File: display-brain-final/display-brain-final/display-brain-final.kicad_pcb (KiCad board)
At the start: 2 copper layers, 104.2 x 68 mm, 22 parts, among them J1 Conn_01x02_Socket, J2 Conn_01x05_Socket, J3 Conn_01x19_Socket, J4 Conn_01x19_Socket, J5 Conn_01x04_Socket, J6 Conn_01x05_Socket, J7 Conn_01x02_Socket, P1 USB_C_Plug_USB2.0, U3 AMS1117CD-3.3

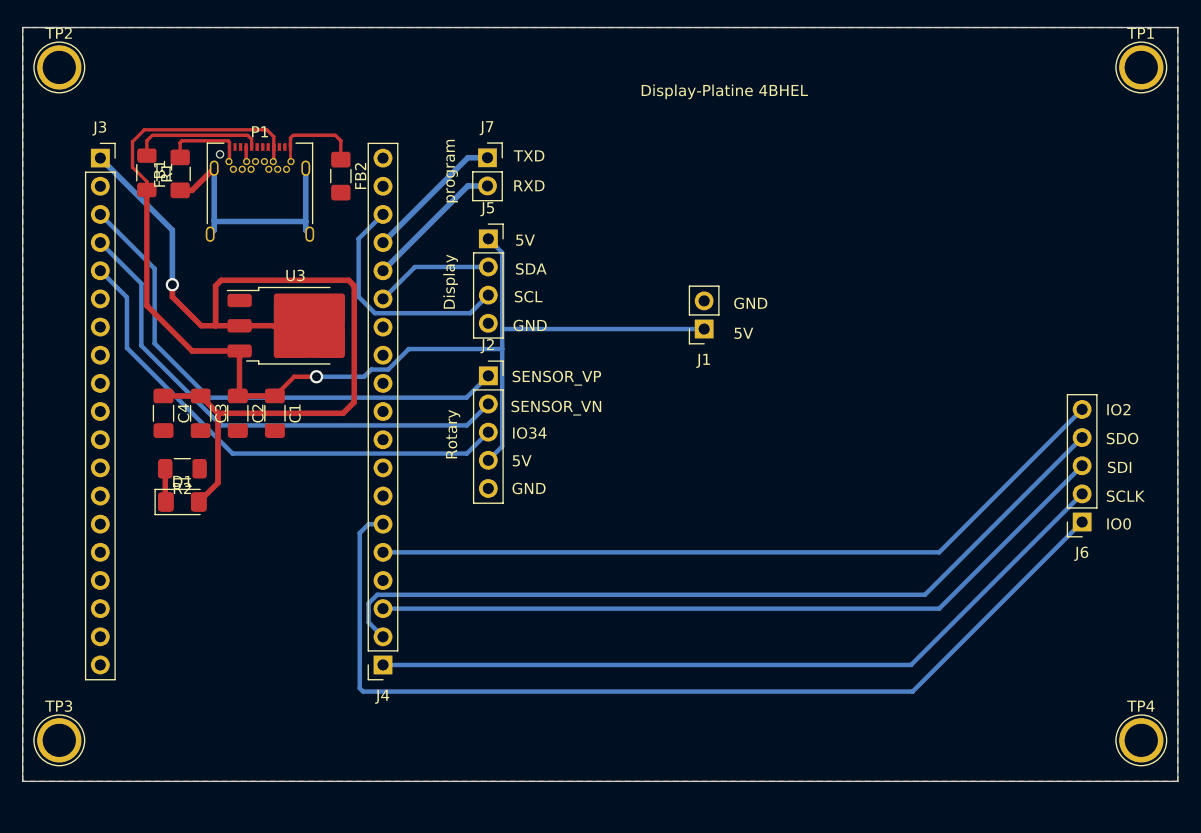
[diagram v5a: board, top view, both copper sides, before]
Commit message: Replaced ASM1117 with LM317 in schematic.
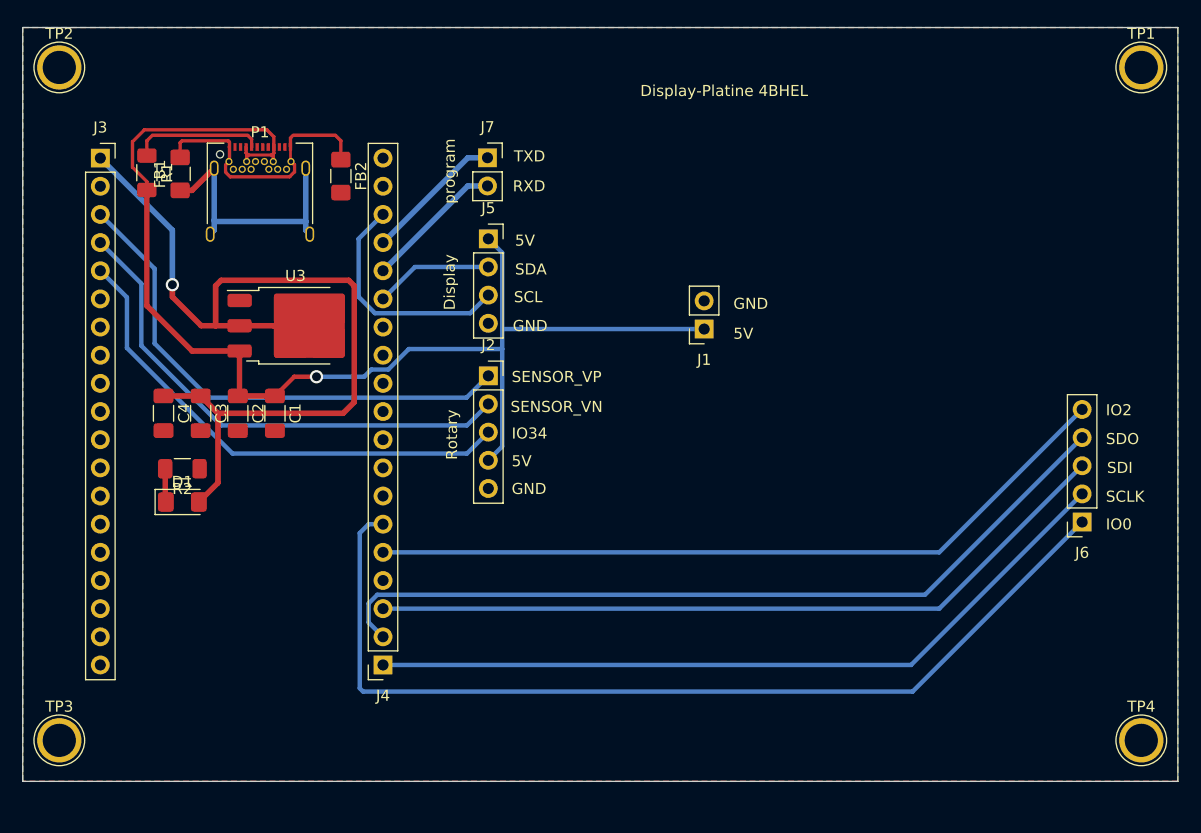
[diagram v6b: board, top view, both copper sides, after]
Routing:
- net Net-(FB1-Pad2): track 16.4 -> 25.0 mm
- net /5V: track 111.4 -> 113.5 mm
- net /SD1: track 69.0 -> 68.4 mm
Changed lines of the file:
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@@
   (segment (start 140.47 58.92) (end 140.3 59.09) (width 0.3) (layer "F.Cu") (net 2))
   (segment (start 140.3 59.09) (end 140.3 60.4125) (width 0.3) (layer "F.Cu") (net 2))
+  (segment (start 144.7 60.79) (end 144.399 61.091) (width 0.3) (layer "F.Cu") (net 2))
   (segment (start 150.25 58.665) (end 150.495 58.42) (width 0.3) (layer "F.Cu") (net 2))
+  (segment (start 150.622 61.087) (end 150.597 61.087) (width 0.3) (layer "F.Cu") (net 2))
+  (segment (start 144.399 61.091) (end 144.399 61.743595) (width 0.3) (layer "F.Cu") (net 2))
   (segment (start 150.495 58.42) (end 154.305 58.42) (width 0.3) (layer "F.Cu") (net 2))
+  (segment (start 150.179 62.165) (end 150.622 61.722) (width 0.3) (layer "F.Cu") (net 2))
   (segment (start 144.75 59.48) (end 144.75 60.74) (width 0.3) (layer "F.Cu") (net 2))
+  (segment (start 150.622 61.722) (end 150.622 61.087) (width 0.3) (layer "F.Cu") (net 2))
   (segment (start 154.305 58.42) (end 154.8 58.915) (width 0.3) (layer "F.Cu") (net 2))
-  (segment (start 144.75 60.74) (end 144.7 60.79) (width 0.3) (layer "F.Cu") (net 2))
+  (segment (start 144.399 61.743595) (end 144.820405 62.165) (width 0.3) (layer "F.Cu") (net 2))
   (segment (start 150.25 60.74) (end 150.25 59.48) (width 0.25) (layer "F.Cu") (net 2))
-  (segment (start 150.3 60.79) (end 150.25 60.74) (width 0.25) (layer "F.Cu") (net 2))
   (segment (start 154.8 58.915) (end 154.8 60.6125) (width 0.3) (layer "F.Cu") (net 2))
   (segment (start 144.75 59.025) (end 144.645 58.92) (width 0.3) (layer "F.Cu") (net 2))
+  (segment (start 150.597 61.087) (end 150.3 60.79) (width 0.3) (layer "F.Cu") (net 2))
   (segment (start 144.75 59.48) (end 144.75 59.025) (width 0.3) (layer "F.Cu") (net 2))
+  (segment (start 144.820405 62.165) (end 150.179 62.165) (width 0.3) (layer "F.Cu") (net 2))
   (segment (start 144.645 58.92) (end 140.47 58.92) (width 0.3) (layer "F.Cu") (net 2))
   (segment (start 150.25 59.48) (end 150.25 58.665) (width 0.3) (layer "F.Cu") (net 2))
@@
   (segment (start 139.6 71.9) (end 139.6 66.98) (width 0.5) (layer "B.Cu") (net 8))
   (segment (start 139.6 66.98) (end 133.1 60.48) (width 0.5) (layer "B.Cu") (net 8))
-  (segment (start 221.427289 90.529879) (end 221.667289 90.769879) (width 0.6) (layer "F.Cu") (net 22))
   (segment (start 206.234336 106.2) (end 221.664578 90.769758) (width 0.4) (layer "B.Cu") (net 22))
   (segment (start 158.6 106.2) (end 206.234336 106.2) (width 0.4) (layer "B.Cu") (net 22))
@@
   (segment (start 157.3 102.36) (end 158.6 103.66) (width 0.4) (layer "B.Cu") (net 23))
   (segment (start 157.3 100.652233) (end 157.3 102.36) (width 0.4) (layer "B.Cu") (net 23))
-  (segment (start 221.267289 87.829879) (end 221.667289 88.229879) (width 0.6) (layer "F.Cu") (net 24))
   (segment (start 221.664578 88.229758) (end 208.774336 101.12) (width 0.4) (layer "B.Cu") (net 24))
   (segment (start 208.774336 101.12) (end 158.6 101.12) (width 0.4) (layer "B.Cu") (net 24))
   (segment (start 208.774336 96.04) (end 158.6 96.04) (width 0.4) (layer "B.Cu") (net 26))
   (segment (start 221.664578 83.149758) (end 208.774336 96.04) (width 0.4) (layer "B.Cu") (net 26))
-  (segment (start 221.567289 93.409879) (end 221.667289 93.309879) (width 0.6) (layer "F.Cu") (net 27))
-  (segment (start 221.567289 93.309879) (end 221.767289 93.109879) (width 0.6) (layer "F.Cu") (net 27))
   (segment (start 206.374336 108.6) (end 156.8 108.6) (width 0.4) (layer "B.Cu") (net 27))
   (segment (start 221.664578 93.309758) (end 206.374336 108.6) (width 0.4) (layer "B.Cu") (net 27))
@@
   (segment (start 148.12 57.92) (end 148.75 58.55) (width 0.3) (layer "F.Cu") (net 39))
   (segment (start 137.3 62.6) (end 136 61.3) (width 0.3) (layer "F.Cu") (net 39))
-  (segment (start 146.25 60.74) (end 146.3 60.79) (width 0.3) (layer "F.Cu") (net 39))
   (segment (start 148.75 58.55) (end 148.75 59.48) (width 0.3) (layer "F.Cu") (net 39))
   (segment (start 148.85 81.9375) (end 145.5 81.9375) (width 0.5) (layer "F.Cu") (net 39))
   (segment (start 137.3 63.35) (end 137.3 62.6) (width 0.3) (layer "F.Cu") (net 39))
+  (segment (start 146.25 59.48) (end 146.25 60.017) (width 0.3) (layer "F.Cu") (net 39))
   (segment (start 145.66 77.88) (end 145.66 81.7775) (width 0.5) (layer "F.Cu") (net 39))
+  (segment (start 146.25 60.017) (end 146.431 60.198) (width 0.3) (layer "F.Cu") (net 39))
   (segment (start 137.3 73.8) (end 137.3 63.35) (width 0.5) (layer "F.Cu") (net 39))
-  (segment (start 145.66 81.7775) (end 145.5 81.9375) (width 0.5) (layer "F.Cu") (net 39))
   (segment (start 136 61.3) (end 136 59) (width 0.3) (layer "F.Cu") (net 39))
-  (segment (start 148.75 60.74) (end 148.7 60.79) (width 0.3) (layer "F.Cu") (net 39))
   (segment (start 150.5875 80.2) (end 148.85 81.9375) (width 0.4) (layer "F.Cu") (net 39))
+  (segment (start 146.3 60.79) (end 146.3 60.329) (width 0.3) (layer "F.Cu") (net 39))
   (segment (start 136 59) (end 137.08 57.92) (width 0.3) (layer "F.Cu") (net 39))
+  (segment (start 148.7 60.308) (end 148.59 60.198) (width 0.3) (layer "F.Cu") (net 39))
   (segment (start 137.08 57.92) (end 148.12 57.92) (width 0.3) (layer "F.Cu") (net 39))
+  (segment (start 148.75 59.48) (end 148.75 60.038) (width 0.3) (layer "F.Cu") (net 39))
   (segment (start 141.38 77.88) (end 137.3 73.8) (width 0.5) (layer "F.Cu") (net 39))
+  (segment (start 146.431 60.198) (end 148.59 60.198) (width 0.3) (layer "F.Cu") (net 39))
+  (segment (start 148.75 60.038) (end 148.59 60.198) (width 0.3) (layer "F.Cu") (net 39))
   (segment (start 145.66 77.88) (end 141.38 77.88) (width 0.5) (layer "F.Cu") (net 39))
-  (segment (start 148.75 59.48) (end 148.75 60.74) (width 0.3) (layer "F.Cu") (net 39))
-  (segment (start 146.25 59.48) (end 146.25 60.74) (width 0.3) (layer "F.Cu") (net 39))
+  (segment (start 148.7 60.79) (end 148.7 60.308) (width 0.3) (layer "F.Cu") (net 39))
   (segment (start 152.6 80.2) (end 150.5875 80.2) (width 0.4) (layer "F.Cu") (net 39))
+  (segment (start 146.3 60.329) (end 146.431 60.198) (width 0.3) (layer "F.Cu") (net 39))
   (via (at 152.6 80.2) (size 1.2) (drill 0.8) (layers "F.Cu" "B.Cu") (net 39))
   (segment (start 157.55 79.55) (end 156.9 80.2) (width 0.4) (layer "B.Cu") (net 39))
@@
   (segment (start 137.3 58.915) (end 137.3 60.25) (width 0.3) (layer "F.Cu") (net 40))
   (segment (start 138.95 88.5) (end 138.95 91.4375) (width 0.5) (layer "F.Cu") (net 48))
-  (segment (start 138.95 91.4375) (end 139.0125 91.5) (width 0.5) (layer "F.Cu") (net 48))
   (zone (net 3) (net_name "GND") (layer "F.Cu") (hatch edge 0.5)
     (connect_pads (clearance 0.5))

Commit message: Updated PCB layout according to new schematic.(ASM1117-> LM317) (Beidl update)
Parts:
- added R3: 1k5, Resistor_SMD:R_1206_3216Metric_Pad1.30x1.75mm_HandSolder, F.Cu at (149.9, 73.3)
- added R4: 910, Resistor_SMD:R_1206_3216Metric_Pad1.30x1.75mm_HandSolder, F.Cu at (151.3, 77.0)
- C2, C3: value 1u -> 100n
- U3: value AMS1117CD-3.3 -> LM317_TO-252; footprint Package_TO_SOT_SMD:TO-252-3_TabPin2 -> Package_TO_SOT_SMD:TO-252-2
- moved C2 10.8 mm to (142.2, 73.2), turned to 180 degrees
- moved C1 10.2 mm to (140.9, 77.0)
- moved R2 10.2 mm to (150.7, 89.3), turned to -90 degrees
- moved D1 7.51 mm to (147.7, 89.3), turned to 90 degrees
- moved U3 7.01 mm to (146.1, 80.9), turned to -90 degrees
- moved C3 6.29 mm to (144.6, 89.3)
- moved C4 6.29 mm to (141.2, 89.3)
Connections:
- U3 pad 1: GND -> Net-(U3-ADJ)
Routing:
- net /3V3: track 81.6 -> 45.9 mm
- net Net-(U3-ADJ): track 0.00 -> 5.69 mm
- net /5V: track 113.5 -> 115.3 mm
